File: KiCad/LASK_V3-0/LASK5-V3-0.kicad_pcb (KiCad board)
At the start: 4 copper layers, 75 x 35 mm, 56 parts, among them IC1 ICM-42688-P, J1 Conn_01x04, J2 JST_02, J3 Conn_01x04_Pin, J4 USB_C_Receptacle, J5 Conn_01x02, J6 Conn_01x06_Pin, J9 Conn_01x04, Q1 IRLML2060, Q2 VP0610T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

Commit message: LASK_V3
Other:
- board text added: "LASK5 V3.0"

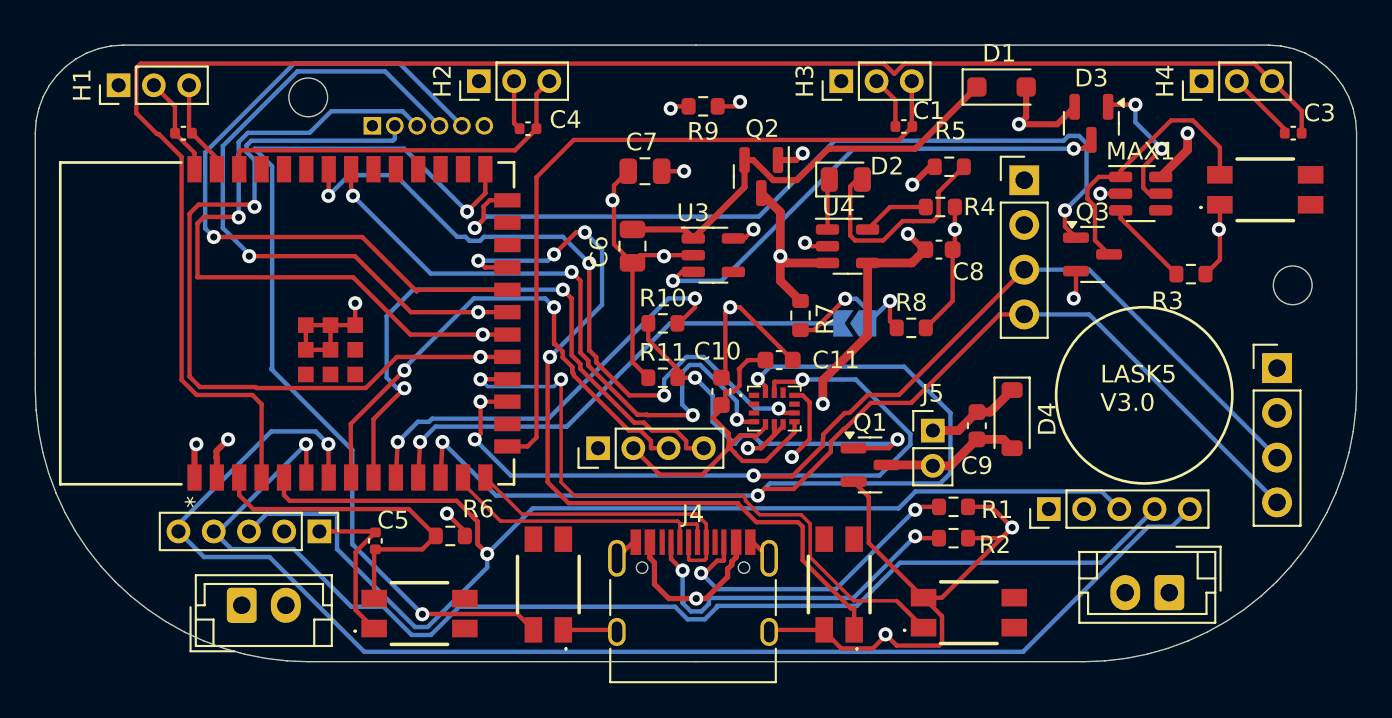
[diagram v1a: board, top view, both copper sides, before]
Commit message: Update LASK5 V3 schematic and PCB; add design backups
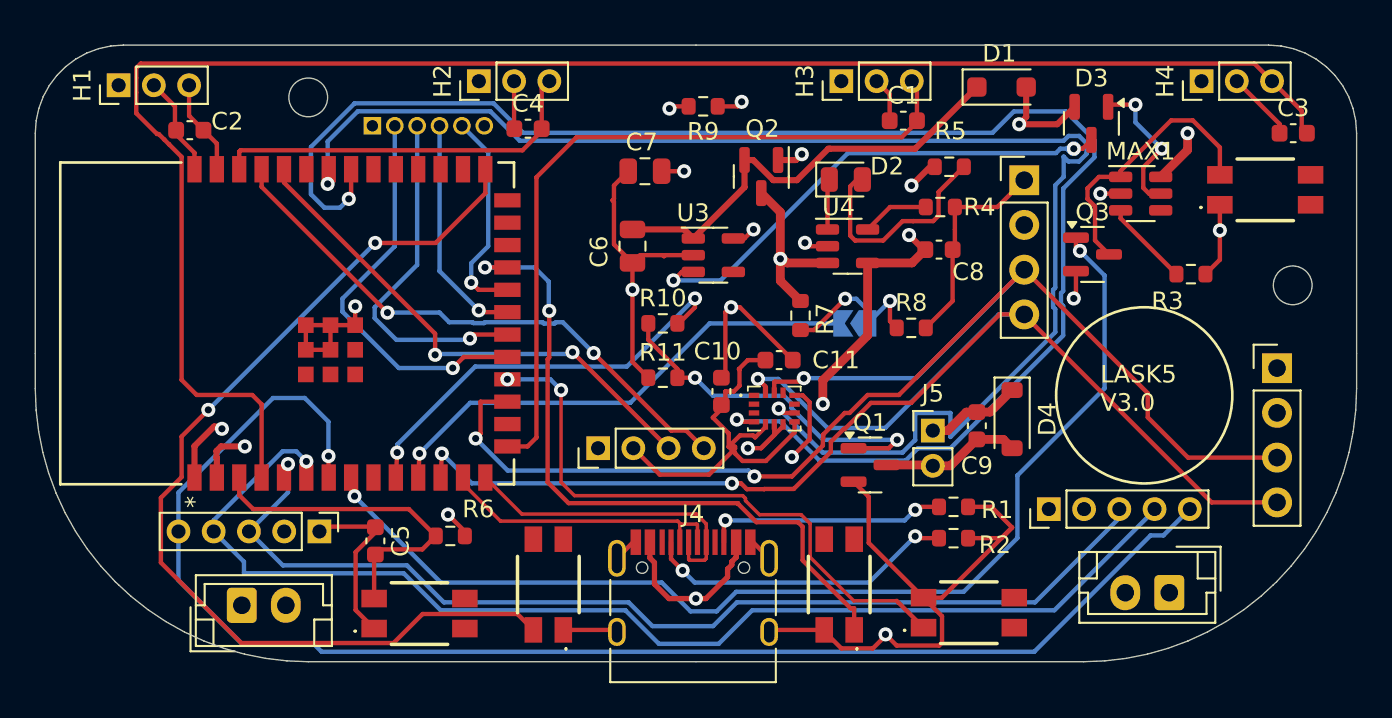
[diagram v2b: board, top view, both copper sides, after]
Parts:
- C1, C2, C3, C4, C5: footprint Capacitor_SMD:C_0402_1005Metric -> Capacitor_SMD:C_0603_1608Metric
- moved C2 0.40 mm to (123.3, 71.0)
- moved C1 0.33 mm to (163.8, 70.4)
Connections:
- J3 pad 3: GP15 -> RX
- J3 pad 4: GP16 -> TX
- U2 pad 26: PWR_OFF -> unconnected-(U2-IO45-Pad26)
- U2 pad 8: GP15 -> PWR_OFF
- U2 pad 9: GP16 -> unconnected-(U2-IO16-Pad9)
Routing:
- net GP33: track 38.1 -> 90.0 mm, vias 4 -> 2
- net GP34: track 39.8 -> 83.9 mm, vias 4 -> 2
- net GP16: track 35.2 -> 0.00 mm, vias 2 -> 0
- net TX: track 0.00 -> 32.4 mm, vias 0 -> 2
- net GP15: track 30.1 -> 0.00 mm, vias 2 -> 0
- net RX: track 0.00 -> 29.7 mm, vias 0 -> 2
- net CS: track 41.1 -> 12.4 mm
- net SPI_MOSI: track 38.3 -> 13.1 mm, vias 2 -> 1
- net SPI_MISO: track 45.2 -> 22.7 mm, vias 2 -> 1
- net SPI_SCK: track 40.0 -> 20.3 mm, vias 2 -> 1
- net PWR_OFF: track 46.1 -> 63.1 mm
- net JX: track 74.9 -> 60.3 mm
- net SDA: track 87.9 -> 78.4 mm
- net MENU: track 47.1 -> 39.4 mm, vias 4 -> 2
- net GND: track 127.8 -> 134.3 mm, vias 15 -> 12
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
